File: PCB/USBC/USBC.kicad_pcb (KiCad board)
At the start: 2 copper layers, 70 x 70 mm, 23 parts, among them J1 USB_A, J2 Shelly, J3 USB-PROG, J4 Conn_01x03_Socket, SW1 SW_Push, U1 VEML6040, U2 ESP32-S3-MINI-1, U5 MD8942

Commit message: USB-C version
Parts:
- removed J1: USB_A, RevK:USB-A-PCB
- added J5: USB_C_Receptacle_USB2.0, RevK:USB_C_SMD_Plug, F.Cu at (112.5, 99.3)
- added R2: 5K1, RevK:R_0402, F.Cu at (109.3, 92.8)
- added R3: 5K1, RevK:R_0402, F.Cu at (109.3, 105.9)
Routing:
- net GND: track 37.0 -> 20.7 mm, vias 15 -> 7
- net D-: track 24.0 -> 39.2 mm, vias 1 -> 2
- net Net-(J5-CC2): track 0.00 -> 8.37 mm, vias 0 -> 2
- net Net-(J5-CC1): track 0.00 -> 6.15 mm
- net VBUS: track 40.4 -> 44.0 mm
- net +3.3V: track 37.6 -> 36.6 mm
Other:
- board text removed: "Glue tab here"

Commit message: Better layout
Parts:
- moved D1 7.40 mm to (112.6, 105.8), turned to 90 degrees
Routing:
- net LED: track 2.26 -> 13.0 mm, vias 0 -> 2
- net VBUS: track 44.0 -> 48.1 mm, vias 2 -> 1
- net GND: track 20.7 -> 17.3 mm, vias 7 -> 14
- net Net-(D1-O): track 3.94 -> 6.83 mm
- net +3.3V: track 36.6 -> 35.7 mm

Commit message: Remove EAN for now
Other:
- board text removed: "5060634238069"

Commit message: Note
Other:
- board text added: "Maybe reverse side plug"
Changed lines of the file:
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@@
   (gr_line (start 87.875 107) (end 112.6 107)
     (stroke (width 0.05) (type default)) (layer "User.2"))
+  (gr_text "Maybe reverse side plug" (at 95.5 90.9) (layer "F.Cu")
+    (effects (font (size 1.5 1.5) (thickness 0.3) bold) (justify left bottom))
+  )
   (gr_text "RGB:12 SCL:34 SDA:48 BTN:42" (at 88.9 106.4) (layer "B.SilkS")
     (effects (font (face "OCR-B") (size 0.7 0.7) (thickness 0.1)) (justify right mirror))

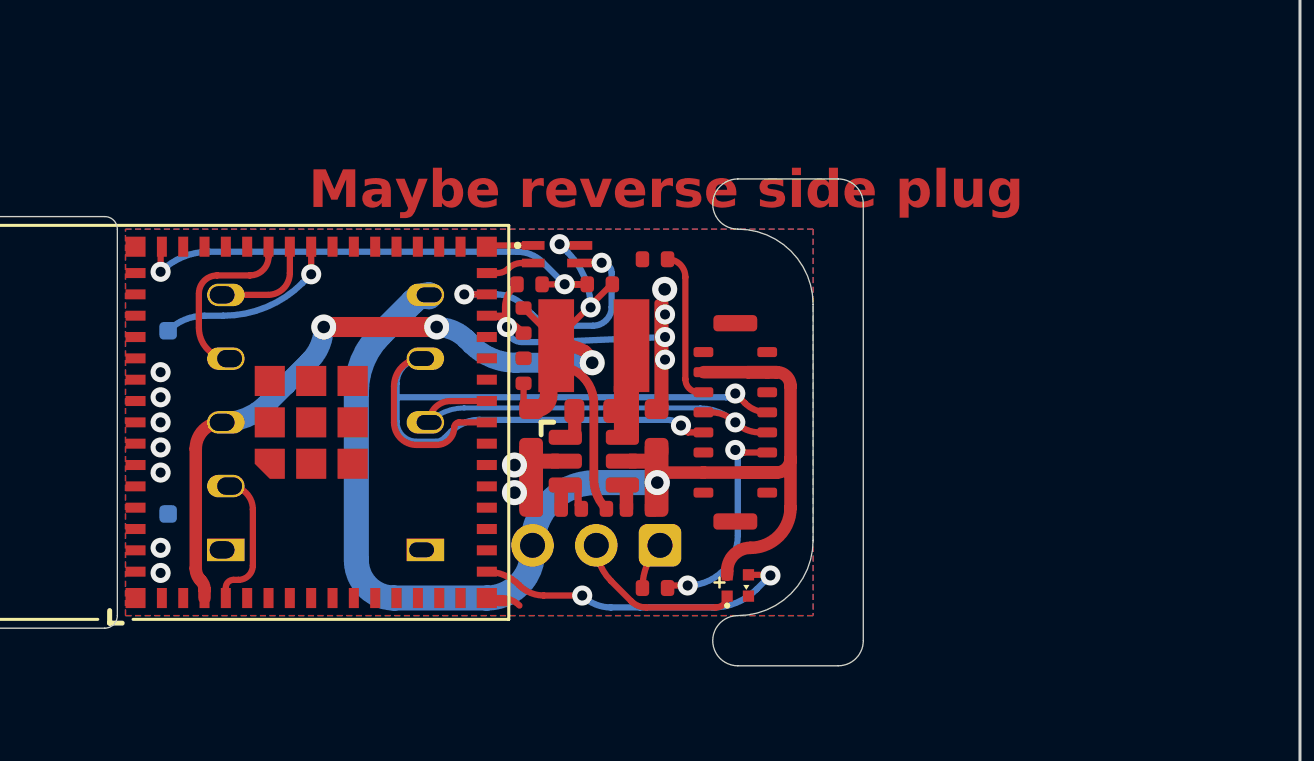
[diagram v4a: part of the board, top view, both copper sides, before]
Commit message: Reworked, double sided (meh), and more LEDs
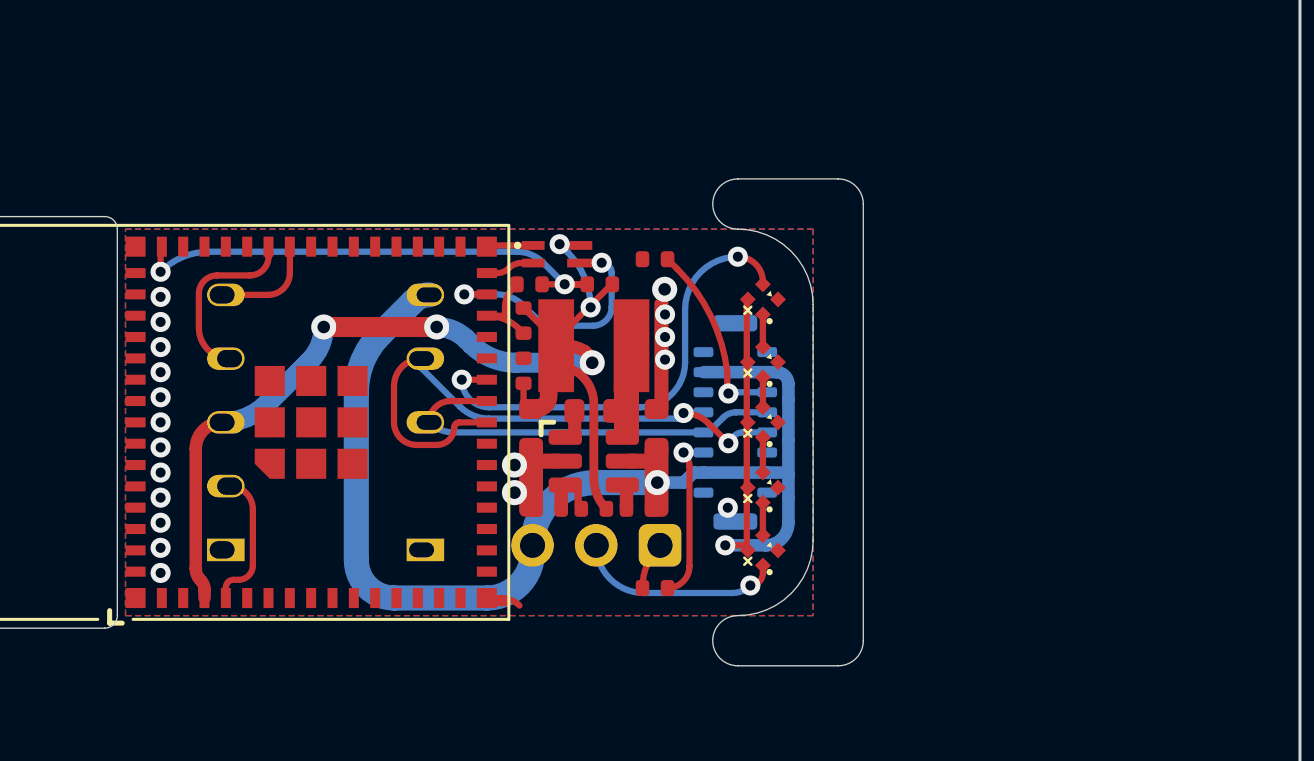
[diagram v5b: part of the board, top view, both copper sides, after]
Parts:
- removed SW1: SW_Push, RevK:TS-1092S-B3D2-G
- added D2: XL-1010RGBC-WS2812B, RevK:SMD1010, F.Cu at (113.6, 96.9)
- added D3: XL-1010RGBC-WS2812B, RevK:SMD1010, F.Cu at (113.6, 99.3)
- added D4: XL-1010RGBC-WS2812B, RevK:SMD1010, F.Cu at (113.6, 101.9)
- added D5: XL-1010RGBC-WS2812B, RevK:SMD1010, F.Cu at (113.6, 104.4)
- J5: moved to B.Cu
- moved D1 11.4 mm to (113.6, 94.4), turned to 135 degrees
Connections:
- J4 pad 2: Net-(D1-O) -> Net-(D5-O)
- U2 pad 16: LED -> unconnected-(U2-GPIO12-Pad16)
- U2 pad 25: unconnected-(U2-GPIO21-Pad25) -> LED
- U2 pad 38: Net-(U2-GPIO42) -> unconnected-(U2-GPIO42-Pad38)
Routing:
- net D-: track 39.2 -> 24.2 mm
- net Net-(D5-O): track 0.00 -> 8.29 mm, vias 0 -> 1
- net GND: track 17.3 -> 9.65 mm, vias 14 -> 19
- net Net-(U2-GPIO42): track 7.42 -> 0.00 mm, vias 1 -> 0
- net VBUS: track 48.1 -> 55.1 mm, vias 1 -> 2
- net Net-(D1-O): track 6.83 -> 1.30 mm
- net LED: track 13.0 -> 18.4 mm
- net Net-(J5-CC1): track 5.95 -> 7.62 mm, vias 0 -> 1
- net Net-(J5-CC2): track 8.36 -> 6.72 mm, vias 2 -> 1
- net Net-(D3-O): track 0.00 -> 1.40 mm
- net D+: track 18.0 -> 16.6 mm, vias 1 -> 0
- net Net-(D4-O): track 0.00 -> 1.30 mm
- net Net-(D2-O): track 0.00 -> 1.20 mm
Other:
- board text added: "RGB:21 SCL:34 SDA:48"
- board text removed: "Maybe reverse side plug"
- board text removed: "RGB:12 SCL:34 SDA:48 BTN:42"

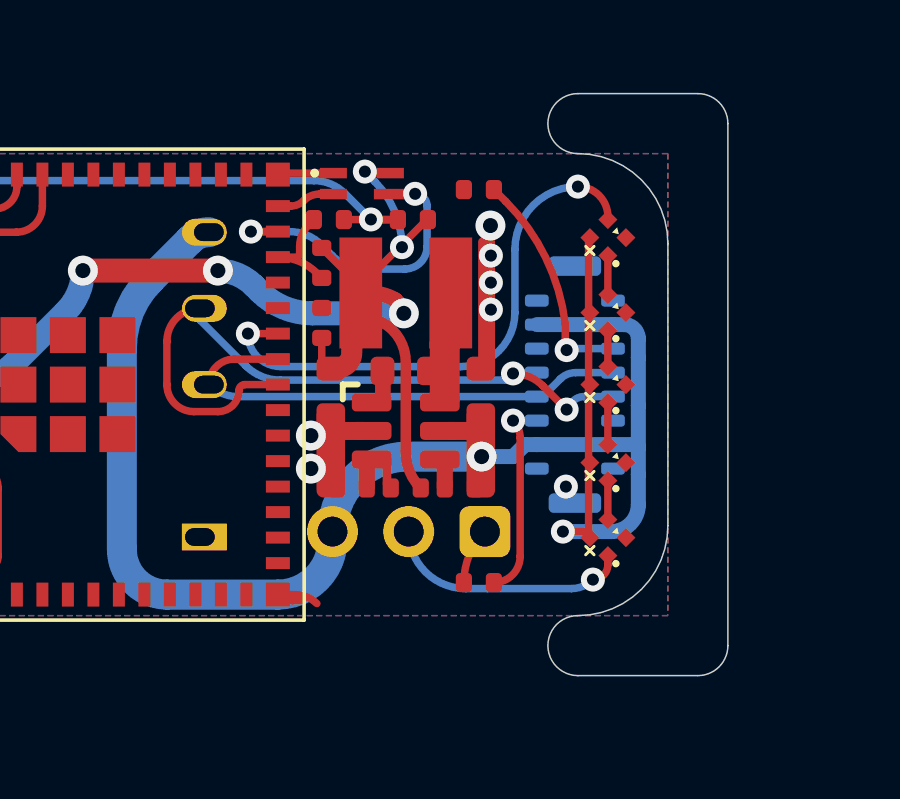
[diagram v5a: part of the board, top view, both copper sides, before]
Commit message: More caps
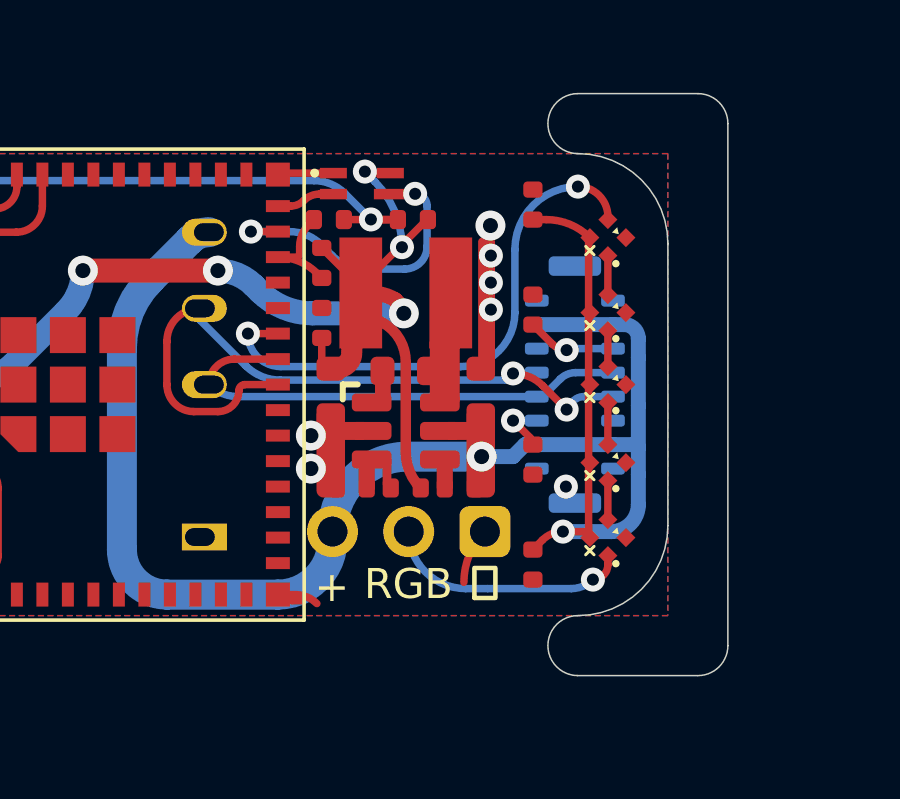
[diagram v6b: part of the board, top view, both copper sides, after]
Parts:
- added C4: 100nF, RevK:C_0402, F.Cu at (111.1, 93.3)
- added C5: 100nF, RevK:C_0402, F.Cu at (111.1, 105.3)
- moved R3 4.48 mm to (111.1, 101.8), turned to -90 degrees
- moved R2 4.39 mm to (111.1, 96.8), turned to 90 degrees
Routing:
- net Net-(J5-CC2): track 6.72 -> 1.85 mm
- net Net-(J5-CC1): track 7.62 -> 3.01 mm
- net VBUS: track 55.1 -> 58.3 mm
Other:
- board text added: "+"
- board text added: "RGB"
- board text added: "⏚"

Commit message: EAN
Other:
- board text added: "5060634238137"
